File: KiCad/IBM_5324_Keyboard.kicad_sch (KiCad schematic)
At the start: 99 parts, among them J1 To 5324, J2 To DB25, SW1 CMD, SW10 ERASE, SW11 | 1, SW12 # 3, SW13 % 5, SW14 & 7, SW15 * +, SW16 ( 9, SW17 _ -, SW18 RH <-, SW19 / -, SW2 ~ `, SW20 NP 8, SW21 HOLD, SW22 FIELD ADV, SW23 W, SW24 R, SW25 Y, SW26 I, SW27 P, SW28 | \, SW29 NP 7, SW3 @ 2, SW30 NP 9, SW31 INQ, SW32 SHIFT LOCK, SW33 Q, SW34 E, SW35 T, SW36 O, SW37 ! ¢, SW38 ENTER, SW39 NP 4, SW4 $ 4, SW40 FIELD-, SW41 U, SW42 ERROR RESET, SW43 LH SHIFT, SW44 A, SW45 D, SW46 G, SW47 J, SW48 L, SW49 " ', SW5 ^ 6, SW50 } {, SW51 NP 5, SW52 NP 6, SW53 TEST, SW54 SCROLL DOWN, SW55 S, SW56 F, SW57 H, SW58 SCROLL UP, SW59 K, SW6 * 8, SW60 : ;, SW61 NEWLINE, SW62 NP 1, SW63 NP 3, SW64 ->, SW65 > <, SW66 C, SW67 B, SW68 M, SW69 . ., SW7 ) 0, SW70 RH SHIFT, SW71 NP 2, SW72 FIELD+, SW73 N, SW74 LH <-, SW75 ALT, SW76 Z, SW77 X, SW78 V, SW79 SPACE, SW8 + =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

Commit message: Design tweaks
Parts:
- U3: footprint Package_DIP:DIP-18_W7.62mm -> Package_DIP:DIP-20_W7.62mm
- renumbered SW16 to SW15, SW17 to SW16, SW18 to SW17, SW20 to SW18, SW21 to SW20, SW22 to SW21, SW23 to SW22, SW24 to SW23, SW25 to SW24, SW26 to SW25, SW27 to SW26, SW28 to SW27, SW29 to SW28, SW30 to SW29, SW31 to SW30, SW32 to SW31, SW33 to SW32, SW34 to SW33, SW35 to SW34, SW41 to SW35, SW42 to SW41, SW43 to SW42, SW44 to SW43, SW45 to SW44, SW46 to SW45, SW47 to SW46, SW48 to SW47, SW49 to SW48, SW50 to SW49, SW51 to SW50, SW52 to SW51, SW53 to SW52, SW54 to SW53, SW55 to SW54, SW56 to SW55, SW57 to SW56, SW59 to SW57, SW60 to SW58, SW61 to SW59, SW62 to SW60, SW63 to SW61, SW58 to SW62, SW64 to SW63, SW65 to SW64, SW66 to SW65, SW67 to SW66, SW73 to SW67, SW74 to SW73, SW75 to SW74, SW76 to SW75, SW77 to SW76, SW78 to SW77, SW79 to SW78, SW80 to SW79, SW81 to SW80, SW82 to SW81, SW83 to SW82, SW84 to SW83, SW15 to SW9
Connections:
- net GND: no longer U1.52 (GND), U1.58 (GND), U1.59 (GND), U1.64 (GND)
- net DATA STROBE_{BUFF} renamed DATA STROB~{E}
- net SCAN CODE BIT 0_{BUFF} renamed SCAN CODE BIT ~{0}
- net SCAN CODE BIT 1_{BUFF} renamed SCAN CODE BIT ~{1}
- net SCAN CODE BIT 2_{BUFF} renamed SCAN CODE BIT ~{2}
- net SCAN CODE BIT 3_{BUFF} renamed SCAN CODE BIT ~{3}
- net SCAN CODE BIT 4_{BUFF} renamed SCAN CODE BIT ~{4}
- net SCAN CODE BIT 5_{BUFF} renamed SCAN CODE BIT ~{5}
- net SCAN CODE BIT 6_{BUFF} renamed SCAN CODE BIT ~{6}
- no-connect marks 22 -> 36
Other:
- moved on the sheet: SW1, SW10, SW11, SW12, SW13, SW14, SW15, SW16, SW17, SW18, SW19, SW2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

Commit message: Swapped DB25 female to male
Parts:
- removed J1: To 5324, Clueless_Engineer:L77SDB25SA4CH4F, symbol Connector:DB25_Socket_MountingHoles
- added D1: +5V Power, LED_THT:LED_D5.0mm, symbol Device:LED
- added J1: To 5324, Clueless_Engineer:L717SDB25P1ACH3R, symbol Connector:DB25_Pins_MountingHoles
- added R1: R, Resistor_THT:R_Axial_DIN0207_L6.3mm_D2.5mm_P7.62mm_Horizontal, symbol Device:R
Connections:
- net +12V: now also J1.12
- net +5V: now also R1.1
- net DATA STROB~{E}: now also J1.1
- net DELAY STROBE: now also U1.13 (11_MOSI_CTX1), J1.9; no longer U1.12 (10_CS_MQSR)
- net GND: now also D1.1 (K), J1.0 (PAD), J1.14 (P14), J1.15 (P15), J1.16 (P16), J1.17 (P17), J1.18 (P18), J1.19 (P19), J1.20 (P20), J1.21 (P21), J1.22 (P22), J1.23 (P23), J1.24 (P24), J1.25 (P25)
- net PROGRAM RESET: now also U1.12 (10_CS_MQSR), J1.10; no longer U1.13 (11_MOSI_CTX1)
- net SCAN CODE BIT ~{0}: now also J1.8
- net SCAN CODE BIT ~{1}: now also J1.7
- net SCAN CODE BIT ~{2}: now also J1.6
- net SCAN CODE BIT ~{3}: now also J1.5
- net SCAN CODE BIT ~{4}: now also J1.4
- net SCAN CODE BIT ~{5}: now also J1.3
- net SCAN CODE BIT ~{6}: now also J1.2
- new net: D1.2 (A), R1.2
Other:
- note removed: "WORK IN PROGRESS"
- title: IBM 5324 Keyboard Replacement -> IBM System/23 Datamaster Model 5324 Keyboard Replacement
- moved on the sheet: C1, J2, U2, U3

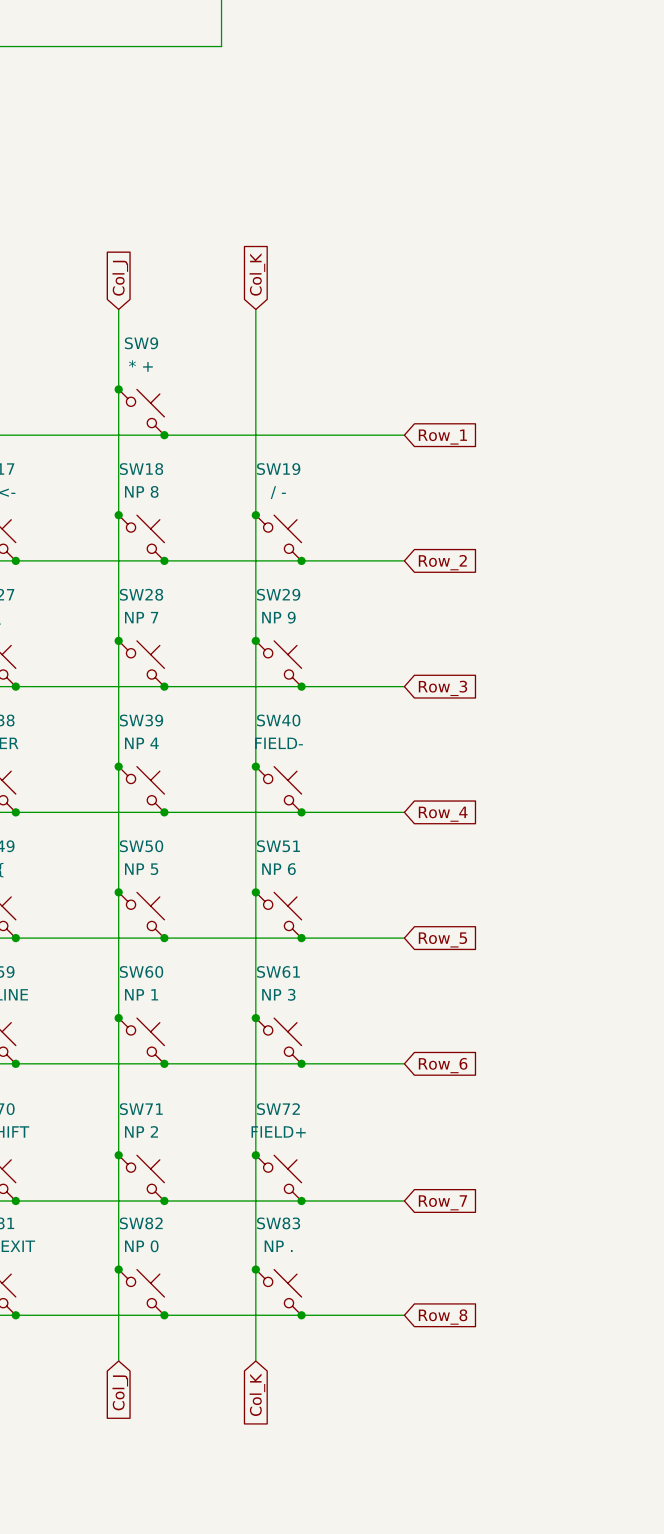
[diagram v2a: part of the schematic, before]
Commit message: Added external pull-up array on rows
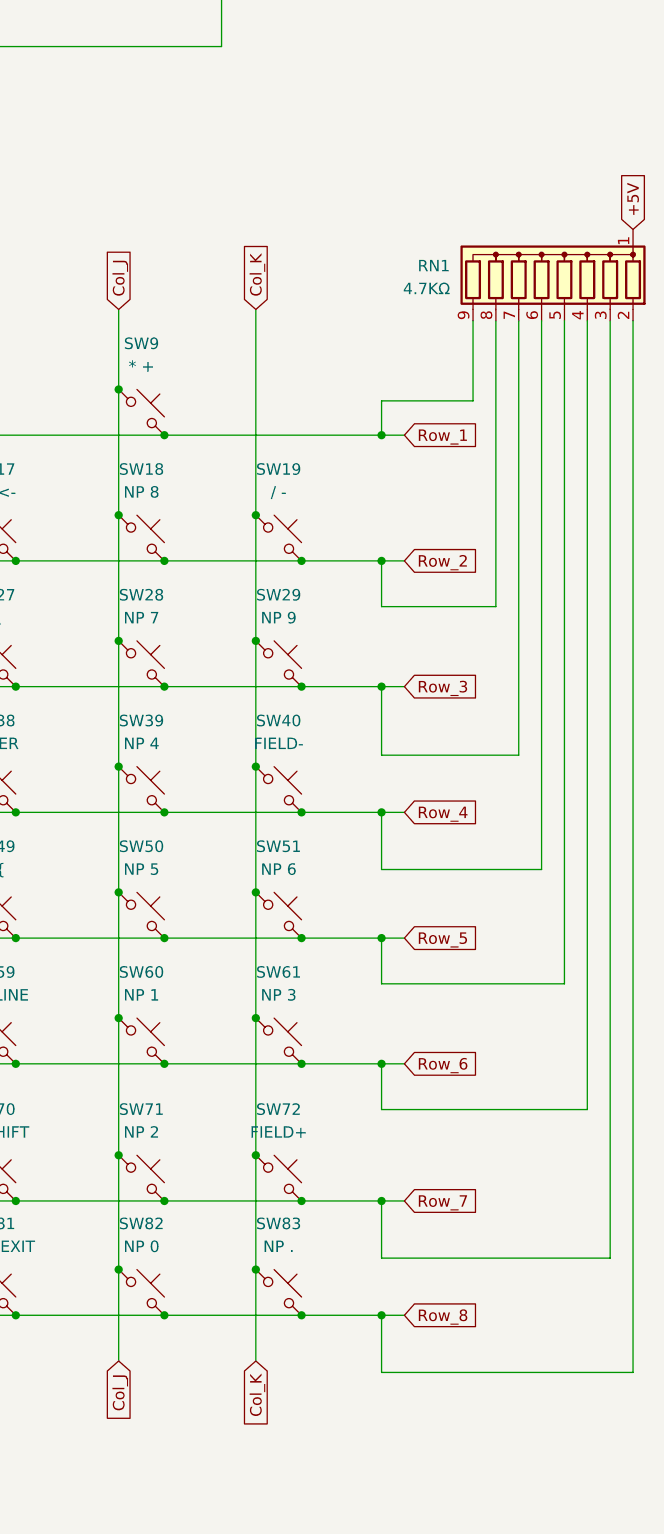
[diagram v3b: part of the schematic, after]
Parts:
- added RN1: 4.7KΩ, Resistor_THT:R_Array_SIP9, symbol Device:R_Network08
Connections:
- net +5V: now also RN1.1 (common)
- net Row_1: now also RN1.9 (R8)
- net Row_2: now also RN1.8 (R7)
- net Row_3: now also RN1.7 (R6)
- net Row_4: now also RN1.6 (R5)
- net Row_5: now also RN1.5 (R4)
- net Row_6: now also RN1.4 (R3)
- net Row_7: now also RN1.3 (R2)
- net Row_8: now also RN1.2 (R1)

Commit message: Revised schematic & PCB layout
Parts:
- added D2: +12V, LED_THT:LED_D5.0mm, symbol Device:LED
- added R2: R, Resistor_THT:R_Axial_DIN0207_L6.3mm_D2.5mm_P7.62mm_Horizontal, symbol Device:R
- D1: value +5V Power -> +5V
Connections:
- net DATA STROB~{E} is gone; now on net DATA STROBE: J1.1, J2.B1 (DATA_STROBE), U3.11 (B7)
- net SCAN CODE BIT ~{0} is gone; now on net SCAN CODE BIT 0: J1.8, J2.B9 (SCAN_CODE_BIT_0), U3.18 (B0)
- net SCAN CODE BIT ~{1} is gone; now on net SCAN CODE BIT 1: J1.7, J2.B8 (SCAN_CODE_BIT_1), U3.17 (B1)
- net SCAN CODE BIT ~{2} is gone; now on net SCAN CODE BIT 2: J1.6, J2.B7 (SCAN_CODE_BIT_2), U3.16 (B2)
- net SCAN CODE BIT ~{3} is gone; now on net SCAN CODE BIT 3: J1.5, J2.B6 (SCAN_CODE_BIT_3), U3.15 (B3)
- net SCAN CODE BIT ~{4} is gone; now on net SCAN CODE BIT 4: J1.4, J2.B5 (SCAN_CODE_BIT_4), U3.14 (B4)
- net SCAN CODE BIT ~{5} is gone; now on net SCAN CODE BIT 5: J1.3, J2.B4 (SCAN_CODE_BIT_5), U3.13 (B5)
- net SCAN CODE BIT ~{6} is gone; now on net SCAN CODE BIT 6: J1.2, J2.B3 (SCAN_CODE_BIT_6), U3.12 (B6)
- net +12V: now also R2.1
- net DATA STROBE: no longer U1.11 (9_OUT1C), U3.9 (A7)
- net GND: now also D2.1 (K)
- net SCAN CODE BIT 0: no longer U1.4 (2_OUT2), U3.2 (A0)
- net SCAN CODE BIT 1: no longer U1.5 (3_LRCLK2), U3.3 (A1)
- net SCAN CODE BIT 2: no longer U1.6 (4_BCLK2), U3.4 (A2)
- net SCAN CODE BIT 3: no longer U1.7 (5_IN2), U3.5 (A3)
- net SCAN CODE BIT 4: no longer U1.8 (6_OUT1D), U3.6 (A4)
- net SCAN CODE BIT 5: no longer U1.9 (7_RX2_OUT1A), U3.7 (A5)
- net SCAN CODE BIT 6: no longer U1.10 (8_TX2_IN1), U3.8 (A6)
- new net: D2.2 (A), R2.2
- new net DS: U1.11 (9_OUT1C), U3.9 (A7)
- new net SCB1: U1.5 (3_LRCLK2), U3.3 (A1)
- new net SCB2: U1.6 (4_BCLK2), U3.4 (A2)
- new net SCB3: U1.7 (5_IN2), U3.5 (A3)
- new net SCB4: U1.8 (6_OUT1D), U3.6 (A4)
- new net SCB5: U1.9 (7_RX2_OUT1A), U3.7 (A5)
- new net SCB6: U1.10 (8_TX2_IN1), U3.8 (A6)
- new net SCB_{0}: U1.4 (2_OUT2), U3.2 (A0)
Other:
- note added: "2x14 pin header interface to DB25 cable"
- note added: "Columns are pulled high in the MCU and pulsed low when scanned. If a key is pressed that row will be pulled low and the key press registered. The MCU will convert the column/row to a scan code and place this on the bus to the 5324 via the 74HCT245 buffer."
- note added: "DB25 male interface to 5324 via DB25 female-male extension cable."
- note added: "Output signals to 5324 are buffered to ensure logic highs are accurately read by the 5324."
- note added: "Replacement for Intel 8048 microcontroller. Converts the col/row matrix to 5324 scan codes."
- note added: "Rows pulled high by default, no key press. Will register low when column is scanned and key is pressed."
- note added: "Unbuffered signals for 5324"
- moved on the sheet: C1, D1, H1, H2, H3, H4, H5, H6, H7, H8, J1, J2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
